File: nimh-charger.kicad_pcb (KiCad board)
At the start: 2 copper layers, 90 x 90 mm, 25 parts, among them J1 PWR_IN

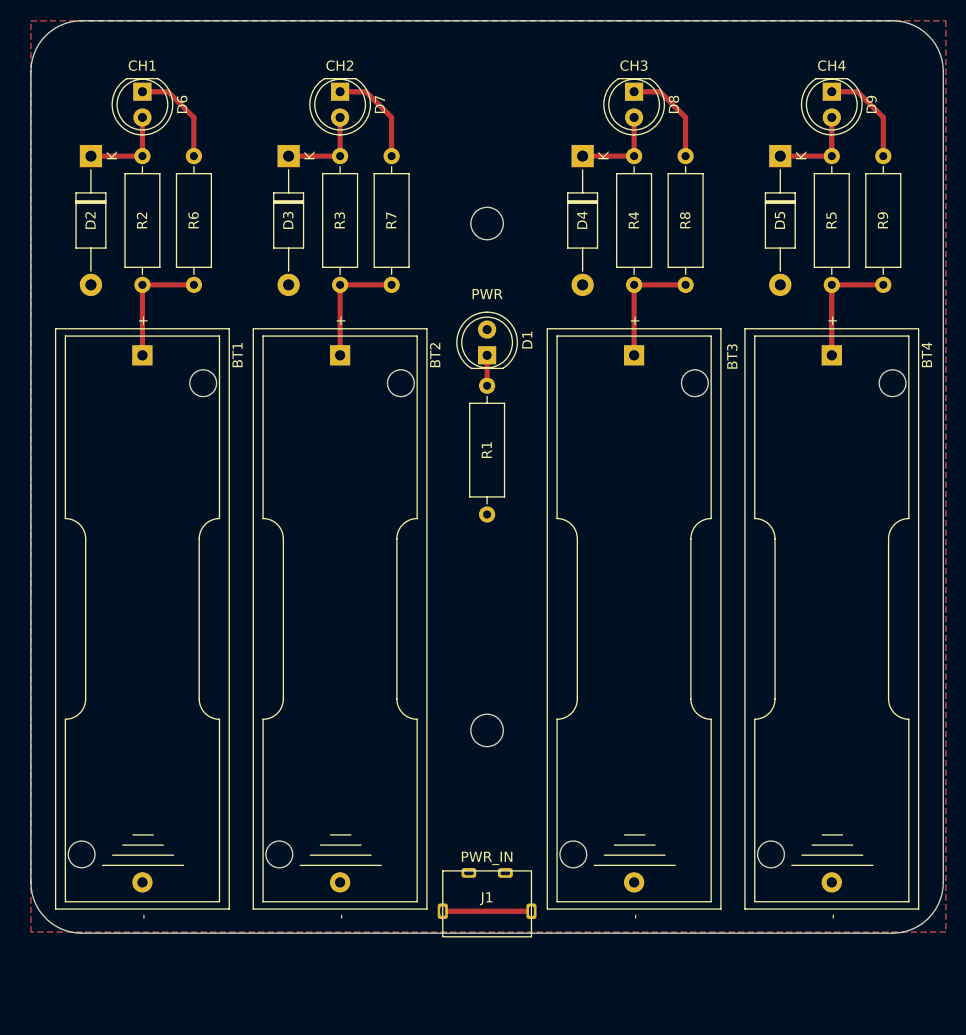
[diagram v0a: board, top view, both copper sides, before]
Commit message: Chonkier pads on resistors for hand soldering, also wider tracks
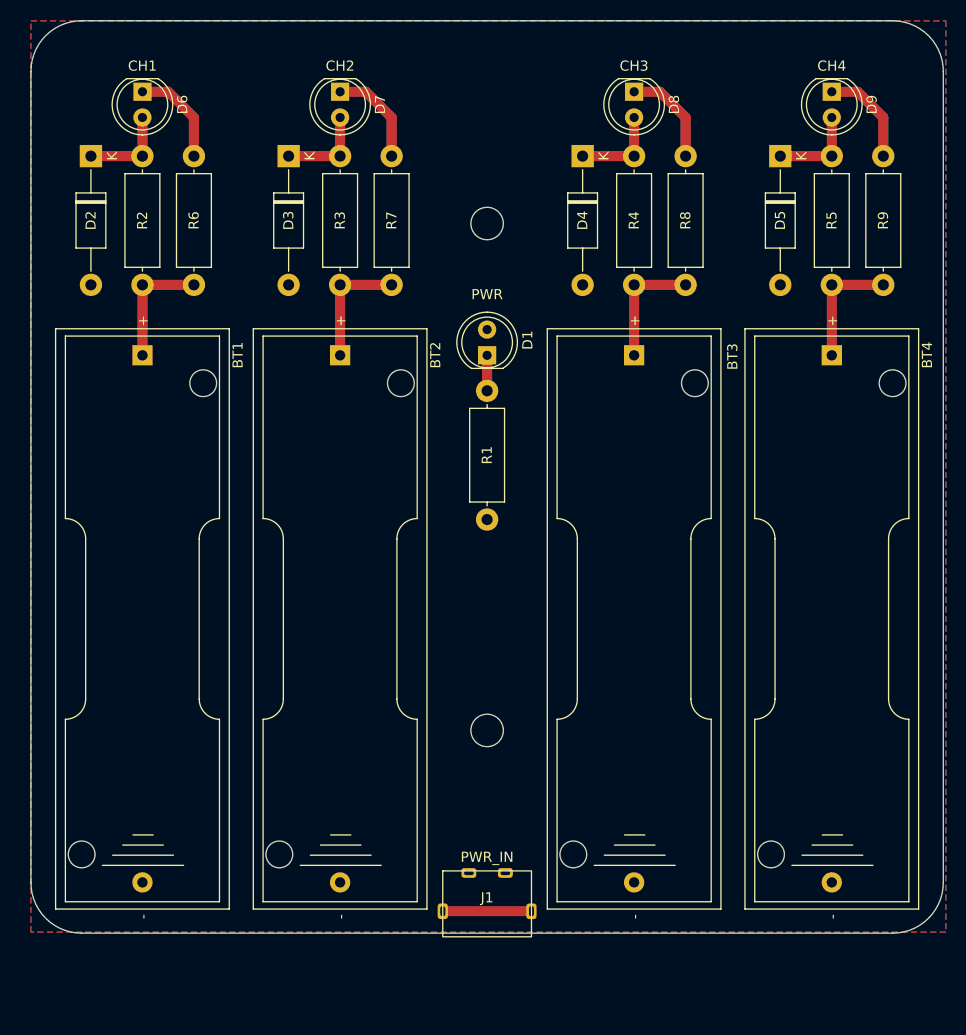
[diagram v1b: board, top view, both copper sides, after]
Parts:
- R1, R2, R3, R4, R5, R6, R7, R8, R9: footprint Resistor_THT:R_Axial_DIN0309_L9.0mm_D3.2mm_P12.70mm_Horizontal -> nimh-charger:R_Axial_DIN0309_L9.0mm_D3.2mm_P12.70mm_Horizontal
- moved R1 0.50 mm to (95.0, 96.5)
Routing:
- net Net-(D1-Pad1): track 3.00 -> 3.50 mm

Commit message: Final tweaks and silk
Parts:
- added TP1: 5V, Connector_Wire:SolderWire-0.5sqmm_1x01_D0.9mm_OD2.1mm_Relief, B.Cu at (92.0, 126.6)
- added TP2: GND, Connector_Wire:SolderWire-0.5sqmm_1x01_D0.9mm_OD2.1mm_Relief, B.Cu at (98.0, 126.6)
- R1, R2, R3, R4, R5, R6, R7, R8, R9: footprint nimh-charger:R_Axial_DIN0309_L9.0mm_D3.2mm_P12.70mm_Horizontal -> Resistor_THT:R_Axial_DIN0309_L9.0mm_D3.2mm_P12.70mm_Horizontal
- moved H1 10.0 mm to (95.0, 120.0)
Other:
- board text added: "NiMH & Ni-Cd Battery Trickle Charger Thomas Bytheway ghub:HarkonenBade/nimh-charger rev 1 2022-03-25"
- board text added: "Power In: 5V Charge Per Cell: ~24mA"

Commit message: PCB Model and Case
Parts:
- BT1, BT2, BT3, BT4: footprint Battery:BatteryHolder_Keystone_2460_1xAA -> nimh-charger:BatteryHolder_Keystone_2460_1xAA

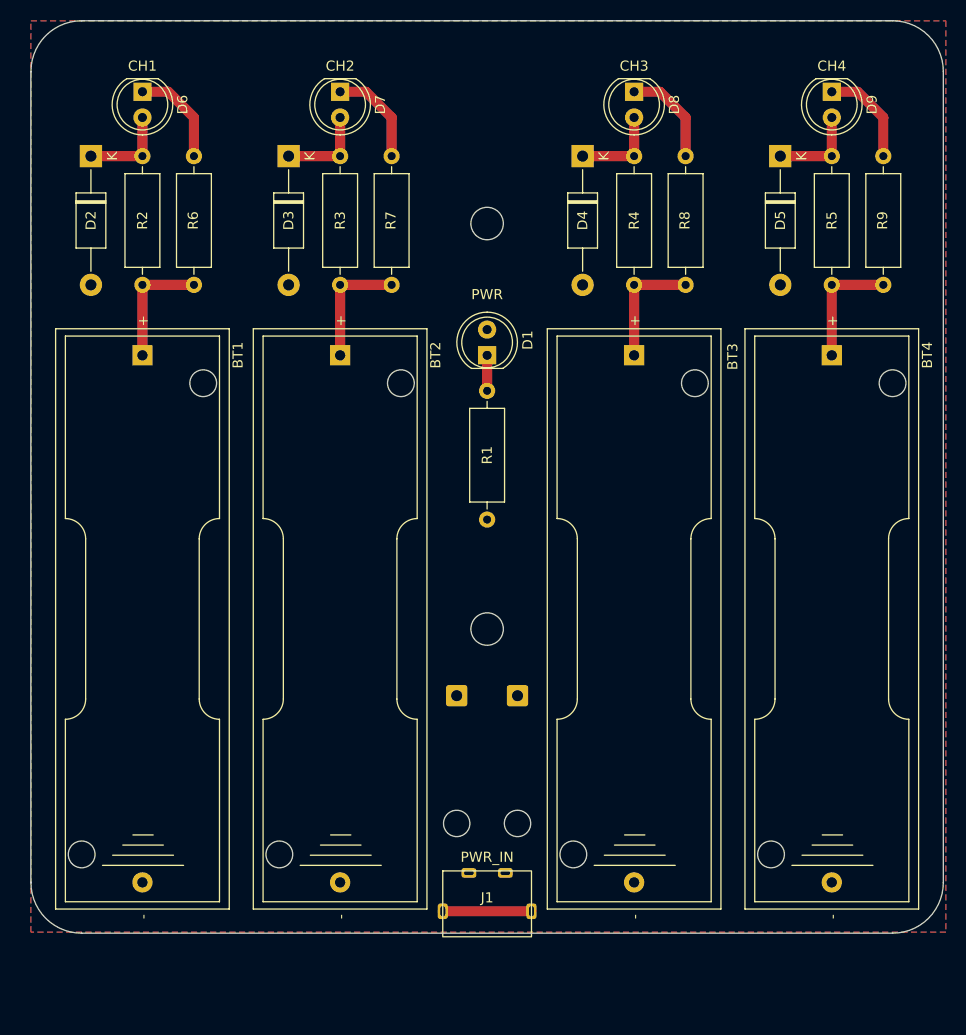
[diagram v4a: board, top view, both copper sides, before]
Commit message: SMD 2-cell chaining version
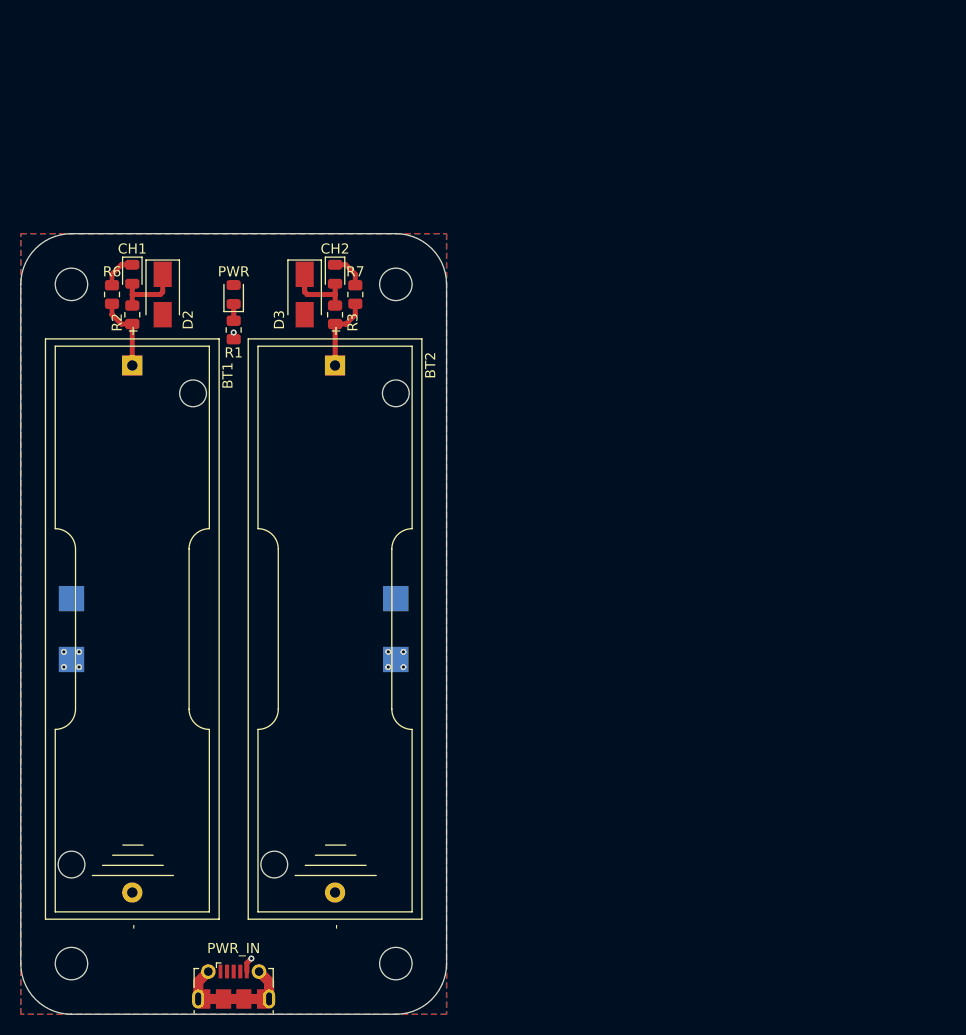
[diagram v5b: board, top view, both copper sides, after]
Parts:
- removed BT3, BT4: Battery_Cell, nimh-charger:BatteryHolder_Keystone_2460_1xAA
- removed D4, D5: 1N400X, Diode_THT:D_DO-41_SOD81_P12.70mm_Horizontal
- removed D8: CH3, LED_THT:LED_D5.0mm
- removed D9: CH4, LED_THT:LED_D5.0mm
- removed R4, R5, R8, R9: 120R, Resistor_THT:R_Axial_DIN0309_L9.0mm_D3.2mm_P12.70mm_Horizontal
- added H3: MountingHole, MountingHole:MountingHole_3.2mm_M3_DIN965, F.Cu at (54.0, 86.0)
- added H4: MountingHole, MountingHole:MountingHole_3.2mm_M3_DIN965, F.Cu at (86.0, 86.0)
- added TP3: 5V, TestPoint:TestPoint_Pad_2.5x2.5mm, B.Cu at (86.0, 123.0)
- added TP4: GND, TestPoint:TestPoint_Pad_2.5x2.5mm, B.Cu at (86.0, 117.0)
- D1, D6, D7: footprint LED_THT:LED_D5.0mm -> LED_SMD:LED_0805_2012Metric
- D2, D3: footprint Diode_THT:D_DO-41_SOD81_P12.70mm_Horizontal -> Diode_SMD:D_SMA
- J1: footprint nimh-charger:KH-TYPE-C-2P -> Connector_USB:USB_Micro-B_Molex-105017-0001
- R1: value 470R -> 1k; footprint Resistor_THT:R_Axial_DIN0309_L9.0mm_D3.2mm_P12.70mm_Horizontal -> Resistor_SMD:R_0805_2012Metric
- R2, R3, R6, R7: footprint Resistor_THT:R_Axial_DIN0309_L9.0mm_D3.2mm_P12.70mm_Horizontal -> Resistor_SMD:R_0805_2012Metric
- TP1, TP2: footprint Connector_Wire:SolderWire-0.5sqmm_1x01_D0.9mm_OD2.1mm_Relief -> TestPoint:TestPoint_Pad_2.5x2.5mm
- moved H2 73.6 mm to (86.0, 153.0)
- moved H1 52.6 mm to (54.0, 153.0)
- moved TP2 45.0 mm to (54.0, 117.0), turned to 0 degrees
- moved TP1 38.2 mm to (54.0, 123.0)
- moved J1 27.4 mm to (70.0, 155.2)
- moved D1 25.7 mm to (70.0, 87.0)
- moved R1 25.7 mm to (70.0, 90.5)
- moved D6 18.0 mm to (60.0, 85.0)
- moved D7 18.0 mm to (80.0, 85.0)
- moved R6 15.9 mm to (58.0, 87.0)
- moved D2 15.4 mm to (63.0, 87.0)
- moved R7 14.1 mm to (82.0, 87.0)
- moved D3 13.7 mm to (77.0, 87.0)
- moved R2 3.11 mm to (60.0, 89.0)
- moved R3 2.99 mm to (80.0, 89.0)
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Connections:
- J1 pad 2: GND -> unconnected-(J1-Pad2)
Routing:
- net unconnected-(J1-Pad6): track 0.00 -> 13.2 mm
- net Net-(BT4-Pad1): track 12.0 -> 0.00 mm
- net Net-(BT3-Pad1): track 12.0 -> 0.00 mm
- net Net-(D9-Pad1): track 9.94 -> 0.00 mm
- net Net-(D8-Pad1): track 9.94 -> 0.00 mm
- net Net-(D5-Pad1): track 8.89 -> 0.00 mm
- net Net-(D4-Pad1): track 8.89 -> 0.00 mm
- net unconnected-(J1-Pad3): track 8.75 -> 0.00 mm
- net Net-(D7-Pad1): track 9.94 -> 3.48 mm
- net Net-(D6-Pad1): track 9.94 -> 3.48 mm
- net Net-(BT1-Pad1): track 12.0 -> 7.55 mm
- net Net-(R3-Pad1): track 12.0 -> 7.55 mm
- net GND: track 0.00 -> 2.14 mm, vias 0 -> 2
- net Net-(D3-Pad1): track 8.89 -> 7.00 mm
- net Net-(D2-Pad1): track 8.89 -> 7.00 mm
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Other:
- board size 90 x 90 mm -> 42 x 77 mm

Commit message: Meltiiing
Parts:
- moved R1 2.01 mm to (70.0, 88.5)
- moved D1 2.00 mm to (70.0, 85.0)
- moved D2 0.25 mm to (62.8, 87.0)
- moved D3 0.25 mm to (77.2, 87.0)
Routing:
- net +5V: track 0.00 -> 1.44 mm, vias 8 -> 9
- net unconnected-(J1-Pad6): track 13.2 -> 12.3 mm
- net Net-(D2-Pad1): track 7.00 -> 7.81 mm
- net Net-(D3-Pad1): track 7.00 -> 7.81 mm
